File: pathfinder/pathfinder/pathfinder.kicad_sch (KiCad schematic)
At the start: 4 parts, among them SW1 SW_Push, SW2 SW_Push, SW3 SW_Push, U1 XIAO-RP2040-DIP

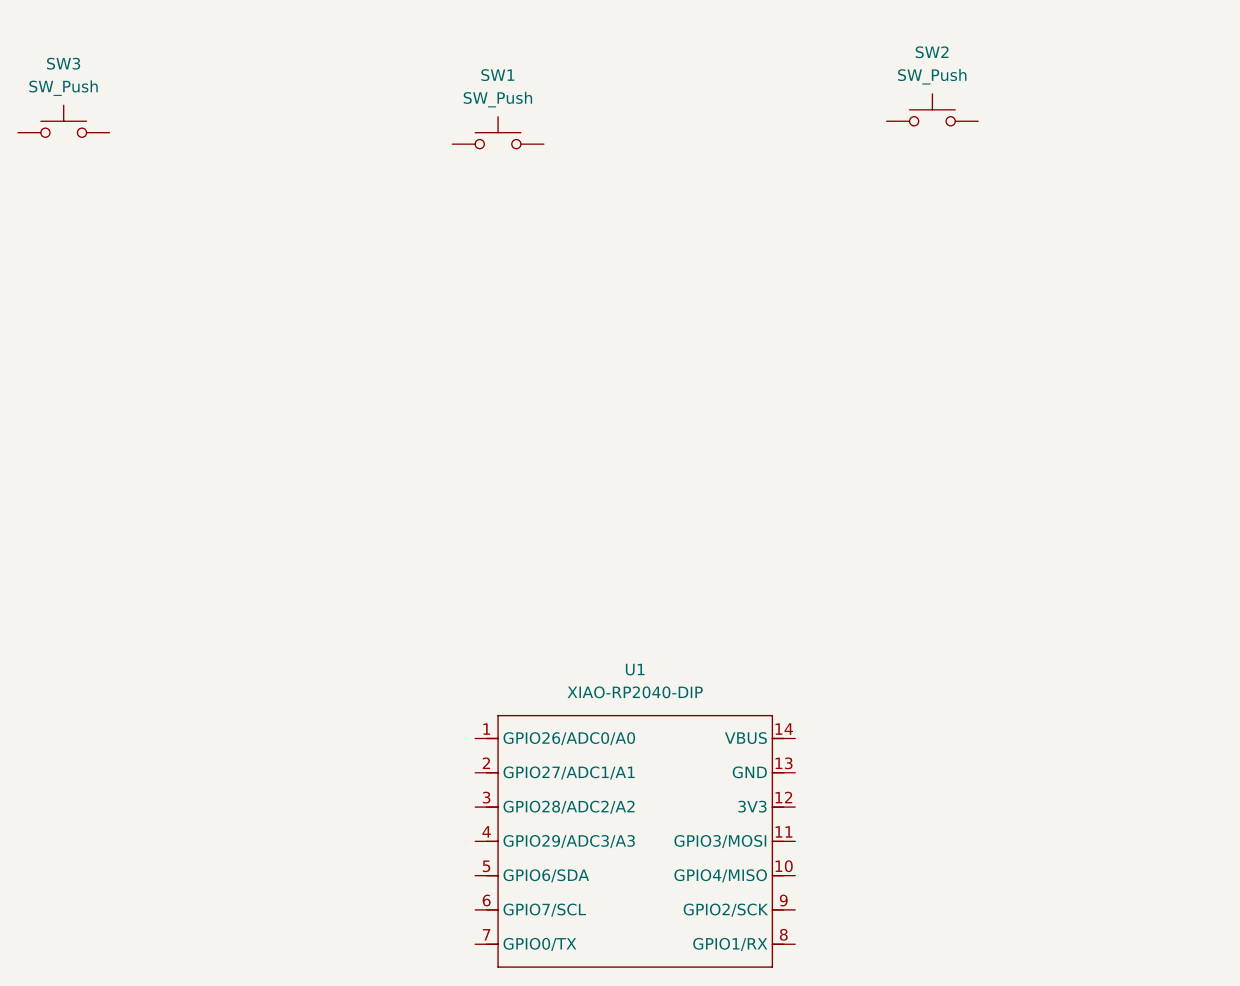
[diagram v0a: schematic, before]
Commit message: Pathfinder update to
Completed pathfinder by adding resistors, wires and a ground
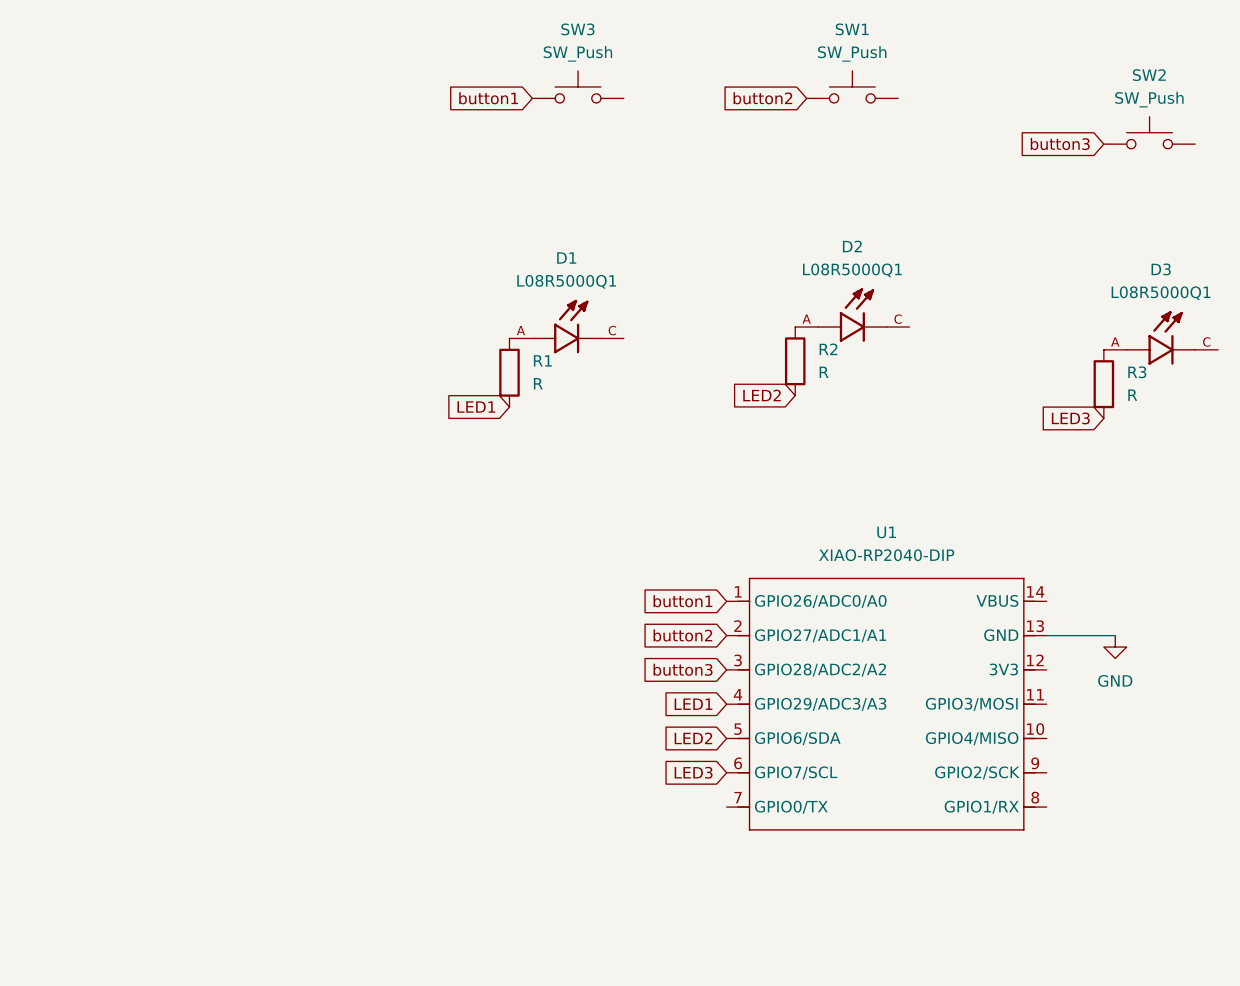
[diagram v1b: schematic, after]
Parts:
- added D1, D2, D3: L08R5000Q1, L08R5000Q1:LEDRD254W57D500H1070, symbol L08R5000Q1:L08R5000Q1
- added R1, R2, R3: R, symbol Device:R
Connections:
- net button2: now reaches SW1.1
- net button2: now also U1.2 (GPIO27/ADC1/A1)
- net button1: now reaches SW3.1
- net button1: now also U1.1 (GPIO26/ADC0/A0)
- net button3: now reaches SW2.1
- net button3: now also U1.3 (GPIO28/ADC2/A2)
- net GND: now reaches U1.13 (GND)
- net LED1: now reaches U1.4 (GPIO29/ADC3/A3)
- net LED1: now also R1.2
- net LED2: now reaches U1.5 (GPIO6/SDA)
- net LED2: now also R2.2
- net LED3: now reaches U1.6 (GPIO7/SCL)
- net LED3: now also R3.2
- new net: D3.A, R3.1
- new net: D2.A, R2.1
- new net: D1.A, R1.1
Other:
- moved on the sheet: SW2, U1
